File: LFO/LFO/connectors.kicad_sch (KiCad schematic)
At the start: 0 parts

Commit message: added missing connectors
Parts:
- added H1, H2, H3, H4: MountingHole_Pad, MountingHole:MountingHole_3.2mm_M3_DIN965_Pad, symbol Mechanical:MountingHole_Pad
- added J1, J3: Conn_01x06, Connector_PinHeader_2.54mm:PinHeader_1x06_P2.54mm_Vertical, symbol Connector_Generic:Conn_01x06
- added J13: Conn_02x05_Odd_Even, Connector_PinHeader_2.54mm:PinHeader_2x05_P2.54mm_Vertical, symbol Connector_Generic:Conn_02x05_Odd_Even
- added J4, J5, J6, J7: Conn_01x01, Connector_PinHeader_2.54mm:PinHeader_1x01_P2.54mm_Vertical, symbol Connector_Generic:Conn_01x01
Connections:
- new net +12V: J13.10 (Pin_10), J13.9 (Pin_9)
- new net -12V: J13.1 (Pin_1), J13.2 (Pin_2)
- new net CFL: J1.1 (Pin_1)
- new net CFV: J1.3 (Pin_3)
- new net CV1: J1.6 (Pin_6)
- new net CV2: J1.5 (Pin_5)
- new net CV3: J1.4 (Pin_4)
- new net FFV: J1.2 (Pin_2)
- new net GND: H1.1, H2.1, H3.1, H4.1, J13.3 (Pin_3), J13.4 (Pin_4), J13.5 (Pin_5), J13.6 (Pin_6), J13.7 (Pin_7), J13.8 (Pin_8)
- new net LEDA: J7.1 (Pin_1)
- new net PW10: J3.5 (Pin_5)
- new net PW90: J3.3 (Pin_3)
- new net PWC: J3.4 (Pin_4)
- new net PWXV: J3.2 (Pin_2)
- new net RMP: J3.1 (Pin_1)
- new net SAW: J5.1 (Pin_1)
- new net SIN: J6.1 (Pin_1)
- new net SQR: J3.6 (Pin_6)
- new net TRI: J4.1 (Pin_1)

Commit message: most of PCB done
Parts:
- removed H3, H4: MountingHole_Pad, MountingHole:MountingHole_3.2mm_M3_DIN965_Pad, symbol Mechanical:MountingHole_Pad
- J1: footprint Connector_PinHeader_2.54mm:PinHeader_1x06_P2.54mm_Vertical -> Connector_PinHeader_2.54mm:PinHeader_1x07_P2.54mm_Vertical; symbol Connector_Generic:Conn_01x06 -> Connector_Generic:Conn_01x07
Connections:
- net CFL: now also J1.2 (Pin_2); no longer J1.1 (Pin_1)
- net CFV: now also J1.4 (Pin_4); no longer J1.3 (Pin_3)
- net CV1: now also J1.7 (Pin_7); no longer J1.6 (Pin_6)
- net CV2: now also J1.6 (Pin_6); no longer J1.5 (Pin_5)
- net CV3: now also J1.5 (Pin_5); no longer J1.4 (Pin_4)
- net FFV: now also J1.3 (Pin_3); no longer J1.2 (Pin_2)
- new net CFH: J1.1 (Pin_1)
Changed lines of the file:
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@@
   (junction (at 195.58 36.83) (diameter 0) (color 0 0 0 0)
   )
-  (junction (at 209.55 111.76) (diameter 0) (color 0 0 0 0)
-  )
   (junction (at 165.1 36.83) (diameter 0) (color 0 0 0 0)
   )
@@
   (junction (at 195.58 39.37) (diameter 0) (color 0 0 0 0)
   )
-  (junction (at 209.55 121.92) (diameter 0) (color 0 0 0 0)
-  )
   (wire (pts (xy 81.28 35.56) (xy 83.82 35.56))
     (stroke (width 0) (type default))
@@
     (stroke (width 0) (type default))
   )
-  (wire (pts (xy 200.66 121.92) (xy 209.55 121.92))
-    (stroke (width 0) (type default))
-  )
   (wire (pts (xy 173.99 31.75) (xy 165.1 31.75))
     (stroke (width 0) (type default))
@@
     (stroke (width 0) (type default))
   )
-  (wire (pts (xy 209.55 125.73) (xy 209.55 121.92))
-    (stroke (width 0) (type default))
-  )
   (wire (pts (xy 200.66 101.6) (xy 209.55 101.6))
     (stroke (width 0) (type default))
@@
     (stroke (width 0) (type default))
   )
+  (wire (pts (xy 77.47 64.77) (xy 80.01 64.77))
+    (stroke (width 0) (type default))
+  )
   (wire (pts (xy 77.47 80.01) (xy 80.01 80.01))
     (stroke (width 0) (type default))
@@
     (stroke (width 0) (type default))
   )
-  (wire (pts (xy 200.66 111.76) (xy 209.55 111.76))
-    (stroke (width 0) (type default))
-  )
   (wire (pts (xy 77.47 97.79) (xy 80.01 97.79))
     (stroke (width 0) (type default))
@@
     (stroke (width 0) (type default))
   )
-  (wire (pts (xy 209.55 111.76) (xy 209.55 101.6))
+  (wire (pts (xy 209.55 101.6) (xy 209.55 105.41))
     (stroke (width 0) (type default))
   )
@@
     (stroke (width 0) (type default))
   )
-  (wire (pts (xy 209.55 121.92) (xy 209.55 111.76))
-    (stroke (width 0) (type default))
-  )
   (wire (pts (xy 77.47 67.31) (xy 80.01 67.31))
     (stroke (width 0) (type default))
@@
     )
   )
+  (global_label "CFH" (shape input) (at 77.47 64.77 180) (fields_autoplaced)
+    (effects (font (size 1.27 1.27)) (justify right))
+    (property "Intersheetrefs" "${INTERSHEET_REFS}" (at 70.7957 64.77 0)
+      (effects (font (size 1.27 1.27)) (justify right) hide)
+    )
+  )
   (global_label "CFV" (shape input) (at 77.47 72.39 180) (fields_autoplaced)
     (effects (font (size 1.27 1.27)) (justify right))
@@
     )
   )
-  (symbol (lib_id "power:GND") (at 209.55 125.73 0) (unit 1)
-    (in_bom yes) (on_board yes) (dnp no) (fields_autoplaced)
-    (property "Reference" "#PWR061" (at 209.55 132.08 0)
-      (effects (font (size 1.27 1.27)) hide)
-    )
-    (property "Value" "GND" (at 209.55 130.81 0)
-      (effects (font (size 1.27 1.27)))
-    )
-    (property "Footprint" "" (at 209.55 125.73 0)
-      (effects (font (size 1.27 1.27)) hide)
-    )
-    (property "Datasheet" "" (at 209.55 125.73 0)
+  (symbol (lib_id "power:GND") (at 209.55 105.41 0) (unit 1)
+    (in_bom yes) (on_board yes) (dnp no) (fields_autoplaced)
+    (property "Reference" "#PWR061" (at 209.55 111.76 0)
+      (effects (font (size 1.27 1.27)) hide)
+    )
+    (property "Value" "GND" (at 209.55 110.49 0)
+      (effects (font (size 1.27 1.27)))
+    )
+    (property "Footprint" "" (at 209.55 105.41 0)
+      (effects (font (size 1.27 1.27)) hide)
+    )
+    (property "Datasheet" "" (at 209.55 105.41 0)
       (effects (font (size 1.27 1.27)) hide)
     )
@@
     )
   )
-  (symbol (lib_id "Connector_Generic:Conn_01x06") (at 85.09 72.39 0) (unit 1)
-    (in_bom yes) (on_board yes) (dnp no) (fields_autoplaced)
-    (property "Reference" "J1" (at 87.63 72.39 0)
-      (effects (font (size 1.27 1.27)) (justify left))
-    )
-    (property "Value" "Conn_01x06" (at 87.63 74.93 0)
-      (effects (font (size 1.27 1.27)) (justify left))
-    )
-    (property "Footprint" "Connector_PinHeader_2.54mm:PinHeader_1x06_P2.54mm_Vertical" (at 85.09 72.39 0)
+  (symbol (lib_id "Connector_Generic:Conn_01x07") (at 85.09 72.39 0) (unit 1)
+    (in_bom yes) (on_board yes) (dnp no) (fields_autoplaced)
+    (property "Reference" "J1" (at 87.63 71.12 0)
+      (effects (font (size 1.27 1.27)) (justify left))
+    )
+    (property "Value" "Conn_01x06" (at 87.63 73.66 0)
+      (effects (font (size 1.27 1.27)) (justify left))
+    )
+    (property "Footprint" "Connector_PinHeader_2.54mm:PinHeader_1x07_P2.54mm_Vertical" (at 85.09 72.39 0)
       (effects (font (size 1.27 1.27)) hide)
     )
@@
     (pin "5")
     (pin "6")
+    (pin "7")
     (instances
       (project "LFO"
@@
         )
       )
-    )
-  )
-  (symbol (lib_id "Mechanical:MountingHole_Pad") (at 198.12 121.92 90) (unit 1)
-    (in_bom yes) (on_board yes) (dnp no) (fields_autoplaced)
-    (property "Reference" "H4" (at 196.85 115.57 90)
-      (effects (font (size 1.27 1.27)))
-    )
-    (property "Value" "MountingHole_Pad" (at 196.85 118.11 90)
-      (effects (font (size 1.27 1.27)))
-    )
-    (property "Footprint" "MountingHole:MountingHole_3.2mm_M3_DIN965_Pad" (at 198.12 121.92 0)
-      (effects (font (size 1.27 1.27)) hide)
-    )
-    (property "Datasheet" "~" (at 198.12 121.92 0)
-      (effects (font (size 1.27 1.27)) hide)
-    )
-    (pin "1")
-    (instances
-      (project "VCA"
-        (path "/a331be11-cf92-4101-a082-e20022c8dee2/105b1da3-69f9-4444-a8b7-56e3901da034"
-          (reference "H4") (unit 1)
-        )
-      )
-      (project "LFO"
-        (path "/acd84bd8-c29a-4e4d-a78d-bbb1d32e037c/764b8532-46b5-43ba-a119-e7e4e00258ed"
-          (reference "H4") (unit 1)
-        )
-      )
-    )
-  )
-  (symbol (lib_id "Mechanical:MountingHole_Pad") (at 198.12 111.76 90) (unit 1)
-    (in_bom yes) (on_board yes) (dnp no) (fields_autoplaced)
-    (property "Reference" "H3" (at 196.85 105.41 90)
-      (effects (font (size 1.27 1.27)))
-    )
-    (property "Value" "MountingHole_Pad" (at 196.85 107.95 90)
-      (effects (font (size 1.27 1.27)))
-    )
-    (property "Footprint" "MountingHole:MountingHole_3.2mm_M3_DIN965_Pad" (at 198.12 111.76 0)
-      (effects (font (size 1.27 1.27)) hide)
-    )
-    (property "Datasheet" "~" (at 198.12 111.76 0)
-      (effects (font (size 1.27 1.27)) hide)
-    )
-    (pin "1")
-    (instances
-      (project "VCA"
-        (path "/a331be11-cf92-4101-a082-e20022c8dee2/105b1da3-69f9-4444-a8b7-56e3901da034"
-          (reference "H3") (unit 1)
-        )
-      )
-      (project "LFO"
-        (path "/acd84bd8-c29a-4e4d-a78d-bbb1d32e037c/764b8532-46b5-43ba-a119-e7e4e00258ed"
-          (reference "H3") (unit 1)
-        )
-      )

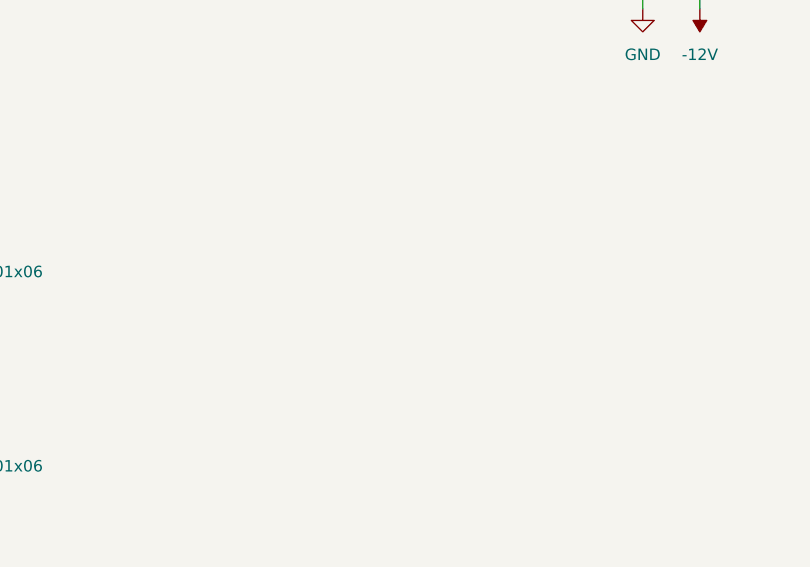
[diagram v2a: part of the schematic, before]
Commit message: added pwr connection to control board
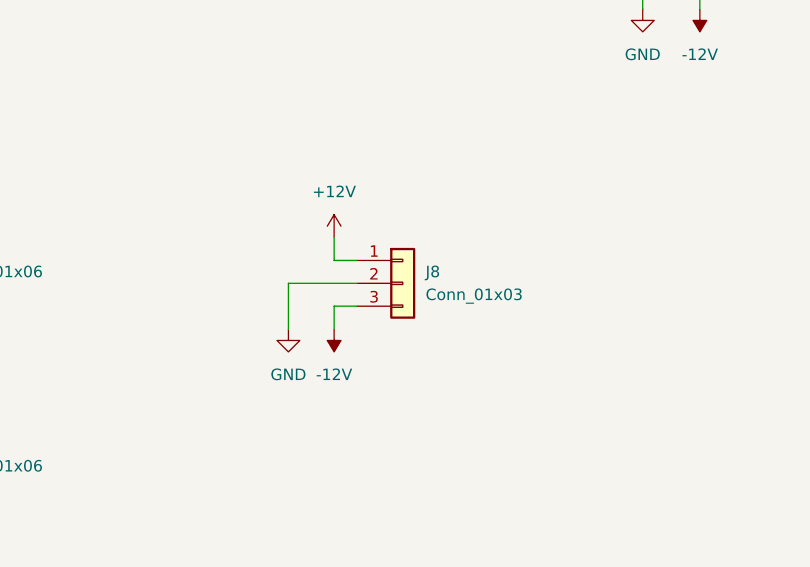
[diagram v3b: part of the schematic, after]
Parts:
- added J8: Conn_01x03, symbol Connector_Generic:Conn_01x03
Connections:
- net +12V: now also J8.1 (Pin_1)
- net -12V: now also J8.3 (Pin_3)
- net GND: now also J8.2 (Pin_2)
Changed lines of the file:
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@@
+    (stroke (width 0) (type default))
+  )
+  (wire (pts (xy 133.35 72.39) (xy 130.81 72.39))
     (stroke (width 0) (type default))
   )
@@
     (stroke (width 0) (type default))
   )
+  (wire (pts (xy 133.35 74.93) (xy 125.73 74.93))
+    (stroke (width 0) (type default))
+  )
   (wire (pts (xy 189.23 41.91) (xy 189.23 44.45))
     (stroke (width 0) (type default))
@@
     (stroke (width 0) (type default))
   )
+  (wire (pts (xy 130.81 72.39) (xy 130.81 69.85))
+    (stroke (width 0) (type default))
+  )
   (wire (pts (xy 209.55 101.6) (xy 209.55 91.44))
     (stroke (width 0) (type default))
@@
     (stroke (width 0) (type default))
   )
+  (wire (pts (xy 130.81 77.47) (xy 130.81 80.01))
+    (stroke (width 0) (type default))
+  )
   (wire (pts (xy 77.47 97.79) (xy 80.01 97.79))
     (stroke (width 0) (type default))
@@
     (stroke (width 0) (type default))
   )
+  (wire (pts (xy 125.73 74.93) (xy 125.73 80.01))
+    (stroke (width 0) (type default))
+  )
+  (wire (pts (xy 133.35 77.47) (xy 130.81 77.47))
+    (stroke (width 0) (type default))
+  )
   (wire (pts (xy 77.47 67.31) (xy 80.01 67.31))
     (stroke (width 0) (type default))
@@
         (path "/acd84bd8-c29a-4e4d-a78d-bbb1d32e037c/764b8532-46b5-43ba-a119-e7e4e00258ed"
           (reference "#PWR057") (unit 1)
+        )
+      )
+    )
+  )
+  (symbol (lib_id "Connector_Generic:Conn_01x03") (at 138.43 74.93 0) (unit 1)
+    (in_bom yes) (on_board yes) (dnp no) (fields_autoplaced)
+    (property "Reference" "J8" (at 140.97 73.66 0)
+      (effects (font (size 1.27 1.27)) (justify left))
+    )
+    (property "Value" "Conn_01x03" (at 140.97 76.2 0)
+      (effects (font (size 1.27 1.27)) (justify left))
+    )
+    (property "Footprint" "" (at 138.43 74.93 0)
+      (effects (font (size 1.27 1.27)) hide)
+    )
+    (property "Datasheet" "~" (at 138.43 74.93 0)
+      (effects (font (size 1.27 1.27)) hide)
+    )
+    (pin "1")
+    (pin "2")
+    (pin "3")
+    (instances
+      (project "LFO"
+        (path "/acd84bd8-c29a-4e4d-a78d-bbb1d32e037c/764b8532-46b5-43ba-a119-e7e4e00258ed"
+          (reference "J8") (unit 1)
         )
       )
@@
     )
   )
+  (symbol (lib_id "power:GND") (at 125.73 80.01 0) (unit 1)
+    (in_bom yes) (on_board yes) (dnp no) (fields_autoplaced)
+    (property "Reference" "#PWR054" (at 125.73 86.36 0)
+      (effects (font (size 1.27 1.27)) hide)
+    )
+    (property "Value" "GND" (at 125.73 85.09 0)
+      (effects (font (size 1.27 1.27)))
+    )
+    (property "Footprint" "" (at 125.73 80.01 0)
+      (effects (font (size 1.27 1.27)) hide)
+    )
+    (property "Datasheet" "" (at 125.73 80.01 0)
+      (effects (font (size 1.27 1.27)) hide)
+    )
+    (pin "1")
+    (instances
+      (project "VCO"
+        (path "/07047393-d9d5-4686-952a-e5b55e75d5c3/da6756ce-4aab-446d-9318-b5790d028b73"
+          (reference "#PWR054") (unit 1)
+        )
+      )
+      (project "VCA"
+        (path "/a331be11-cf92-4101-a082-e20022c8dee2/105b1da3-69f9-4444-a8b7-56e3901da034"
+          (reference "#PWR053") (unit 1)
+        )
+      )
+      (project "LFO"
+        (path "/acd84bd8-c29a-4e4d-a78d-bbb1d32e037c/764b8532-46b5-43ba-a119-e7e4e00258ed"
+          (reference "#PWR059") (unit 1)
+        )
+      )
+    )
+  )
   (symbol (lib_id "Connector_Generic:Conn_01x06") (at 85.09 92.71 0) (unit 1)
     (in_bom yes) (on_board yes) (dnp no) (fields_autoplaced)
@@
         (path "/acd84bd8-c29a-4e4d-a78d-bbb1d32e037c/764b8532-46b5-43ba-a119-e7e4e00258ed"
           (reference "#PWR056") (unit 1)
+        )
+      )
+    )
+  )
+  (symbol (lib_id "power:+12V") (at 130.81 69.85 0) (unit 1)
+    (in_bom yes) (on_board yes) (dnp no) (fields_autoplaced)
+    (property "Reference" "#PWR053" (at 130.81 73.66 0)
+      (effects (font (size 1.27 1.27)) hide)
+    )
+    (property "Value" "+12V" (at 130.81 64.77 0)
+      (effects (font (size 1.27 1.27)))
+    )
+    (property "Footprint" "" (at 130.81 69.85 0)
+      (effects (font (size 1.27 1.27)) hide)
+    )
+    (property "Datasheet" "" (at 130.81 69.85 0)
+      (effects (font (size 1.27 1.27)) hide)
+    )
+    (pin "1")
+    (instances
+      (project "VCO"
+        (path "/07047393-d9d5-4686-952a-e5b55e75d5c3/da6756ce-4aab-446d-9318-b5790d028b73"
+          (reference "#PWR053") (unit 1)
+        )
+      )
+      (project "VCA"
+        (path "/a331be11-cf92-4101-a082-e20022c8dee2/105b1da3-69f9-4444-a8b7-56e3901da034"
+          (reference "#PWR052") (unit 1)
+        )
+      )
+      (project "LFO"
+        (path "/acd84bd8-c29a-4e4d-a78d-bbb1d32e037c/764b8532-46b5-43ba-a119-e7e4e00258ed"
+          (reference "#PWR058") (unit 1)
         )
       )
@@
         )
       )
+    )
+  )
+  (symbol (lib_id "power:-12V") (at 130.81 80.01 180) (unit 1)
+    (in_bom yes) (on_board yes) (dnp no) (fields_autoplaced)
+    (property "Reference" "#PWR055" (at 130.81 82.55 0)
+      (effects (font (size 1.27 1.27)) hide)
+    )
+    (property "Value" "-12V" (at 130.81 85.09 0)
+      (effects (font (size 1.27 1.27)))
+    )
+    (property "Footprint" "" (at 130.81 80.01 0)
+      (effects (font (size 1.27 1.27)) hide)
+    )
+    (property "Datasheet" "" (at 130.81 80.01 0)
+      (effects (font (size 1.27 1.27)) hide)
+    )
+    (pin "1")
+    (instances
+      (project "VCO"
+        (path "/07047393-d9d5-4686-952a-e5b55e75d5c3/da6756ce-4aab-446d-9318-b5790d028b73"
+          (reference "#PWR055") (unit 1)
+        )
+      )
+      (project "VCA"
+        (path "/a331be11-cf92-4101-a082-e20022c8dee2/105b1da3-69f9-4444-a8b7-56e3901da034"
+          (reference "#PWR054") (unit 1)
+        )
+      )
+      (project "LFO"
+        (path "/acd84bd8-c29a-4e4d-a78d-bbb1d32e037c/764b8532-46b5-43ba-a119-e7e4e00258ed"
+          (reference "#PWR060") (unit 1)
+        )
+      )

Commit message: minor fixes after first build
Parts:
- removed J8: Conn_01x03, symbol Connector_Generic:Conn_01x03
- added J15: Conn_01x03, Connector_PinHeader_2.54mm:PinHeader_1x03_P2.54mm_Vertical, symbol Connector_Generic:Conn_01x03
- renumbered J3 to J2, J7 to LEDA1, J5 to SAW1, J6 to SIN1, J4 to TRI1
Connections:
- net +12V: now also J15.1 (Pin_1)
- net -12V: now also J15.3 (Pin_3)
- net GND: now also J15.2 (Pin_2)
